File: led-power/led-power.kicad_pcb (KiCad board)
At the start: 2 copper layers, 86.4 x 86.4 mm, 88 parts, among them J1 String1, J10 PowerInput, J11 Qwiic, J12 Qwiic, J2 String2, J3 String3, J4 String4, J5 String5, J6 String6, J7 String7, J8 String8, J9 PowerInput, Q1 Q_NMOS_GDS, Q2 Q_NMOS_GDS, Q3 Q_NMOS_GDS, Q4 Q_NMOS_GDS, Q5 Q_NMOS_GDS, Q6 Q_NMOS_GDS, Q7 Q_NMOS_GDS, Q8 Q_NMOS_GDS, U1 MCP6V51, U10 L78L05ACZ-AP, U11 MCP1501, U2 MCP6V51, U3 MCP6V51, U4 MCP6V51, U5 MCP6V51, U6 MCP6V51, U7 MCP6V51, U8 MCP6V51, U9 MCP23017_SO

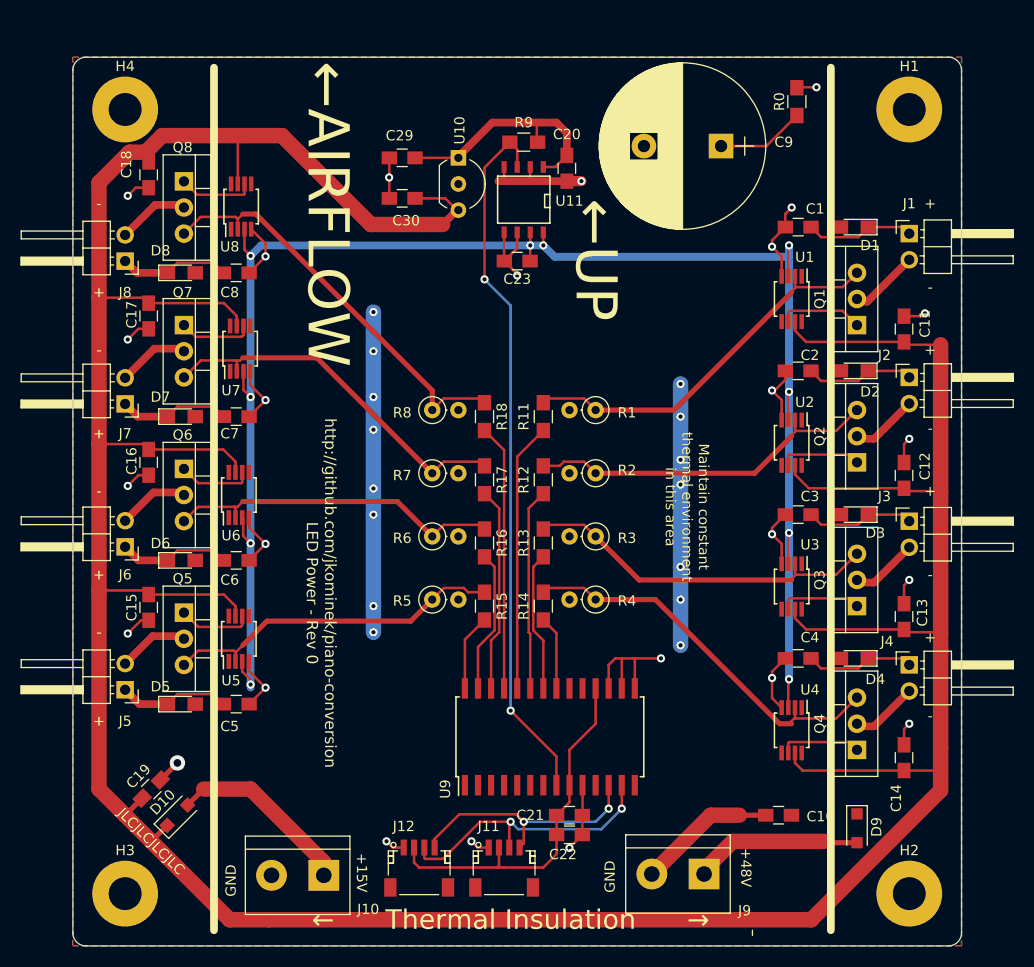
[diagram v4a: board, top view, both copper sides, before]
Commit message: Made I2C address configurable to match other boards, tweaked silkscreen
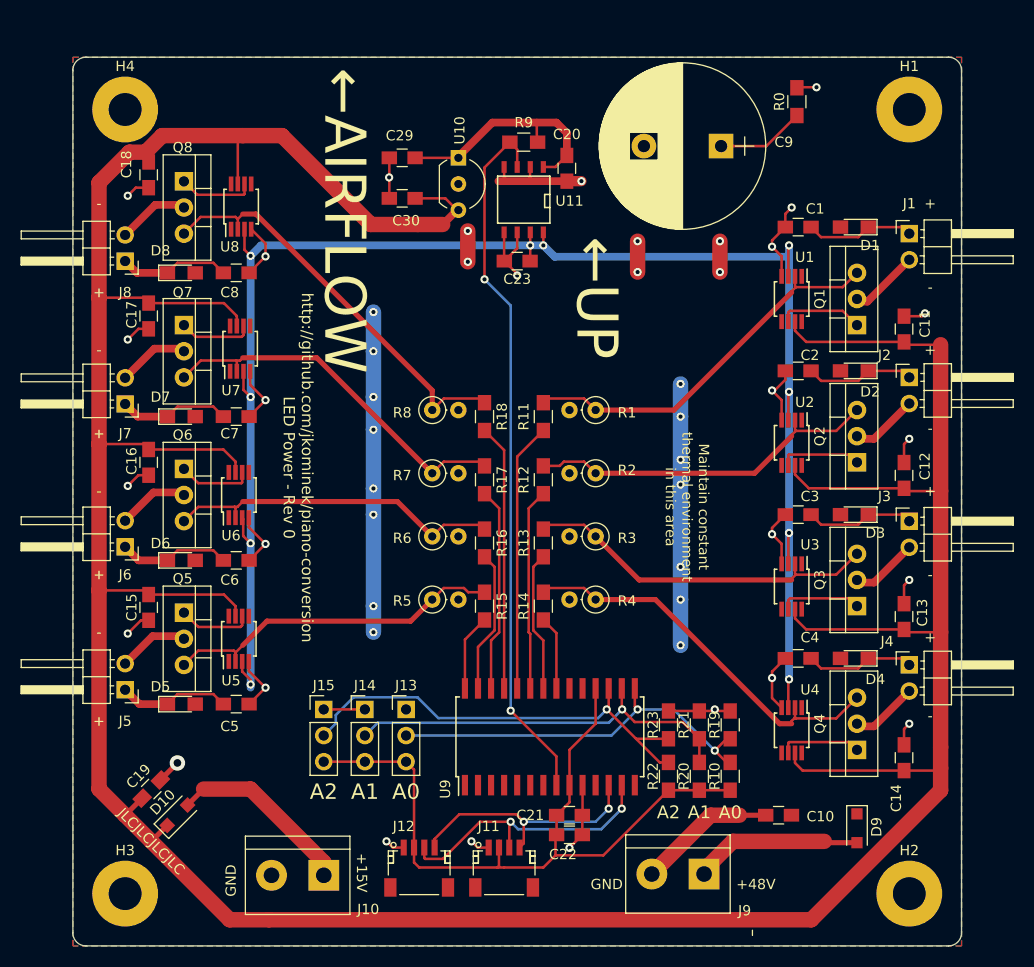
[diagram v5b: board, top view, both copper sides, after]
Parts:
- added J13: A0, Pin_Headers:Pin_Header_Straight_1x03_Pitch2.54mm, F.Cu at (103.5, 134.5)
- added J14: A1, Pin_Headers:Pin_Header_Straight_1x03_Pitch2.54mm, F.Cu at (99.5, 134.5)
- added J15: A2, Pin_Headers:Pin_Header_Straight_1x03_Pitch2.54mm, F.Cu at (95.5, 134.5)
- added R10: DNP, Resistors_SMD:R_0805_HandSoldering, F.Cu at (135.0, 141.0)
- added R19: DNP, Resistors_SMD:R_0805_HandSoldering, F.Cu at (135.0, 136.0)
- added R20: DNP, Resistors_SMD:R_0805_HandSoldering, F.Cu at (132.0, 141.0)
- added R21: DNP, Resistors_SMD:R_0805_HandSoldering, F.Cu at (132.0, 136.0)
- added R22: DNP, Resistors_SMD:R_0805_HandSoldering, F.Cu at (129.0, 141.0)
- added R23: DNP, Resistors_SMD:R_0805_HandSoldering, F.Cu at (129.0, 136.0)
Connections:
- U9 pad 15: GND -> /A0
- U9 pad 16: GND -> /A1
- U9 pad 17: GND -> /A2
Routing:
- net /A2: track 0.00 -> 44.1 mm, vias 0 -> 1
- net /A1: track 0.00 -> 39.1 mm, vias 0 -> 1
- net /A0: track 0.00 -> 38.8 mm, vias 0 -> 2
- net +3V3: track 36.4 -> 72.6 mm
- net GND: track 131.0 -> 136.7 mm, vias 26 -> 32
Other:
- board text added: "A0"
- board text added: "A1"
- board text added: "A2"
- board text removed: "← Thermal Insulation →"

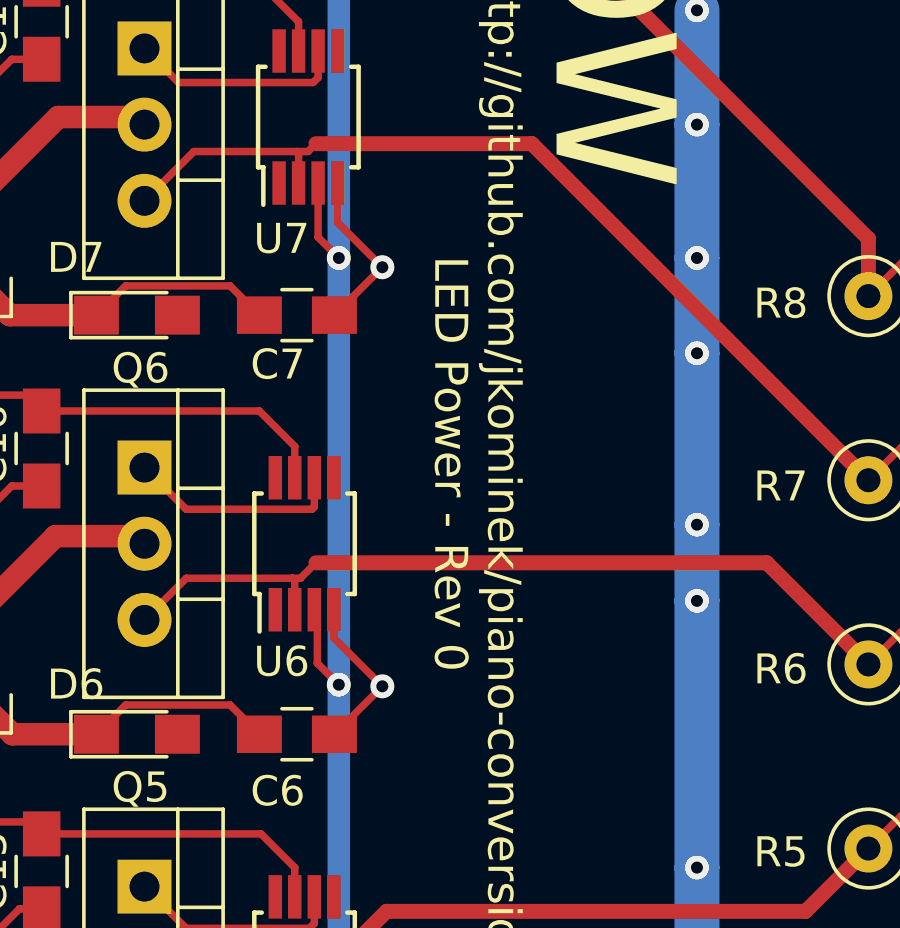
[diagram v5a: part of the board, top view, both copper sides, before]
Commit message: Add/update board rev silkscreen, nothing else
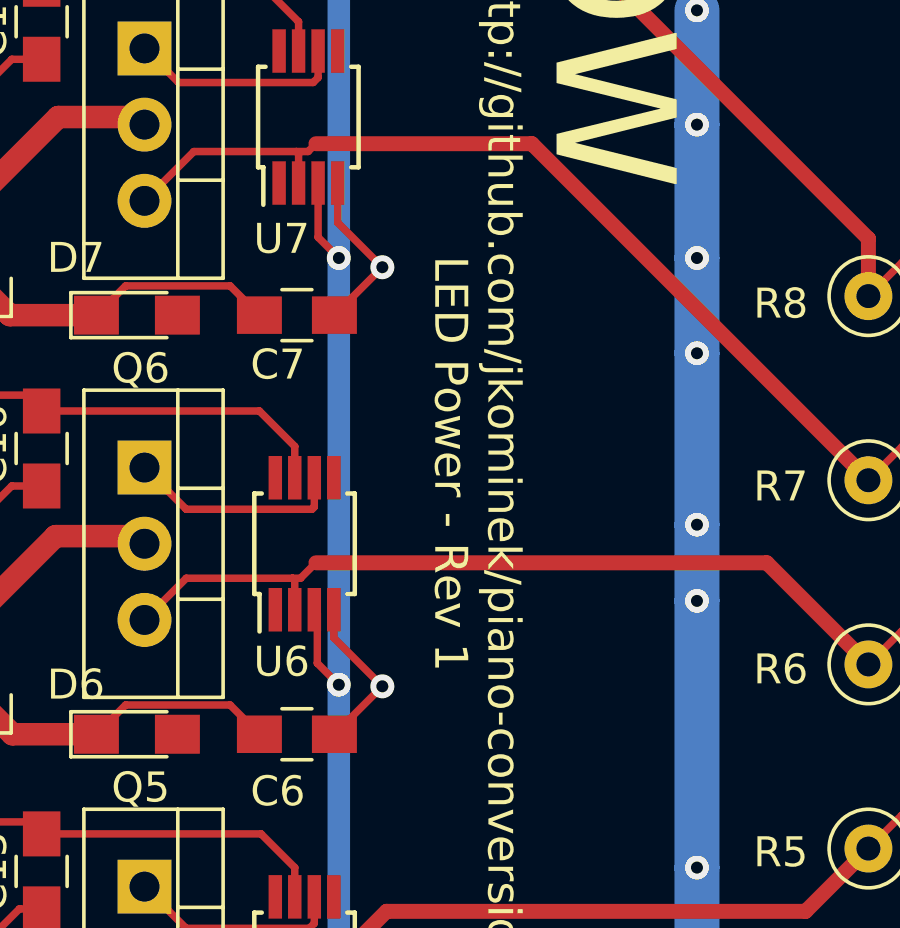
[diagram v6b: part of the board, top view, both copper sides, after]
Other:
- board text added: "http://github.com/jkominek/piano-conversion LED Power - Rev 1"
- board text removed: "http://github.com/jkominek/piano-conversion LED Power - Rev 0"

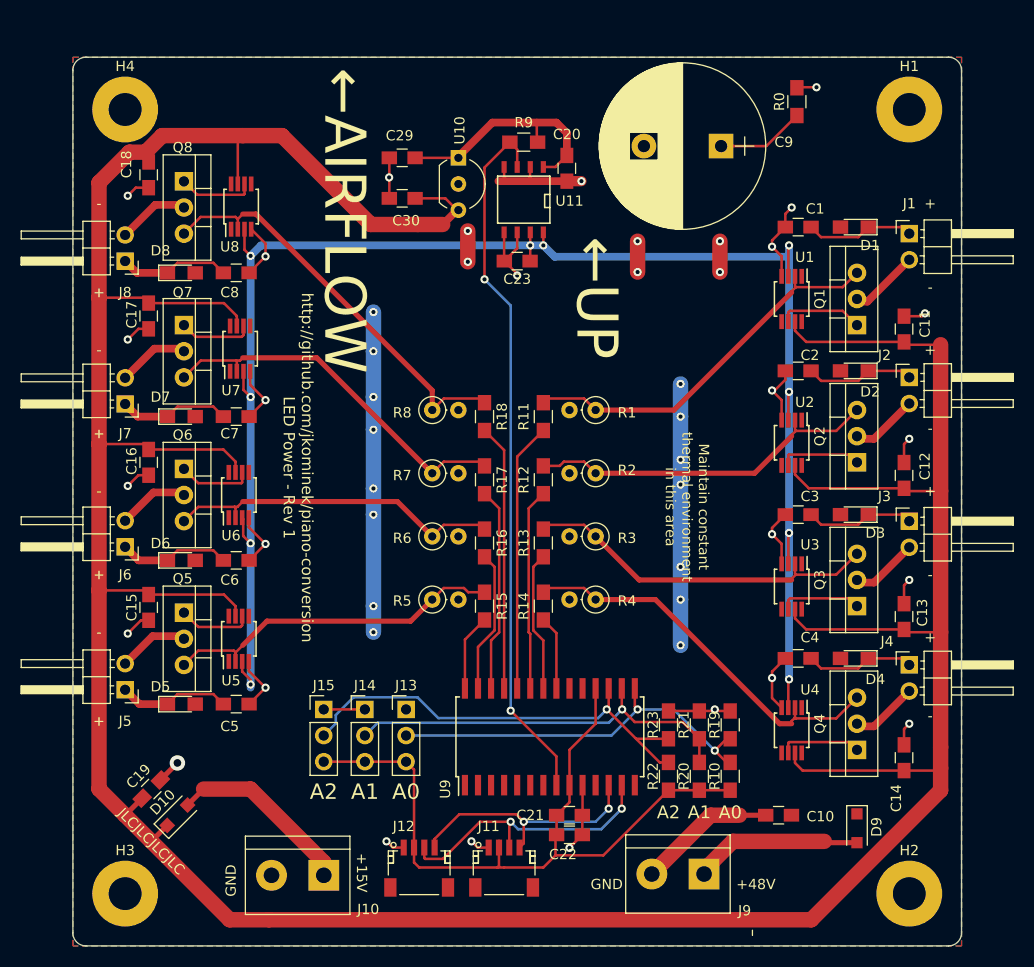
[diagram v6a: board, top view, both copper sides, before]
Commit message: Rev 2 changes
* Pulldown on VREF so that ~SHDN can work
* Voltage dividers on the rails, fed to the MCP23017 so it can detect faults
* Increased space between Qwiic headers
* Bring I2C bus out on 0.100" header
* Tweaked LED positions on the left side; right seemed to be fine.
* Converted it to a four layer board. +15V/GND/GND/+48V
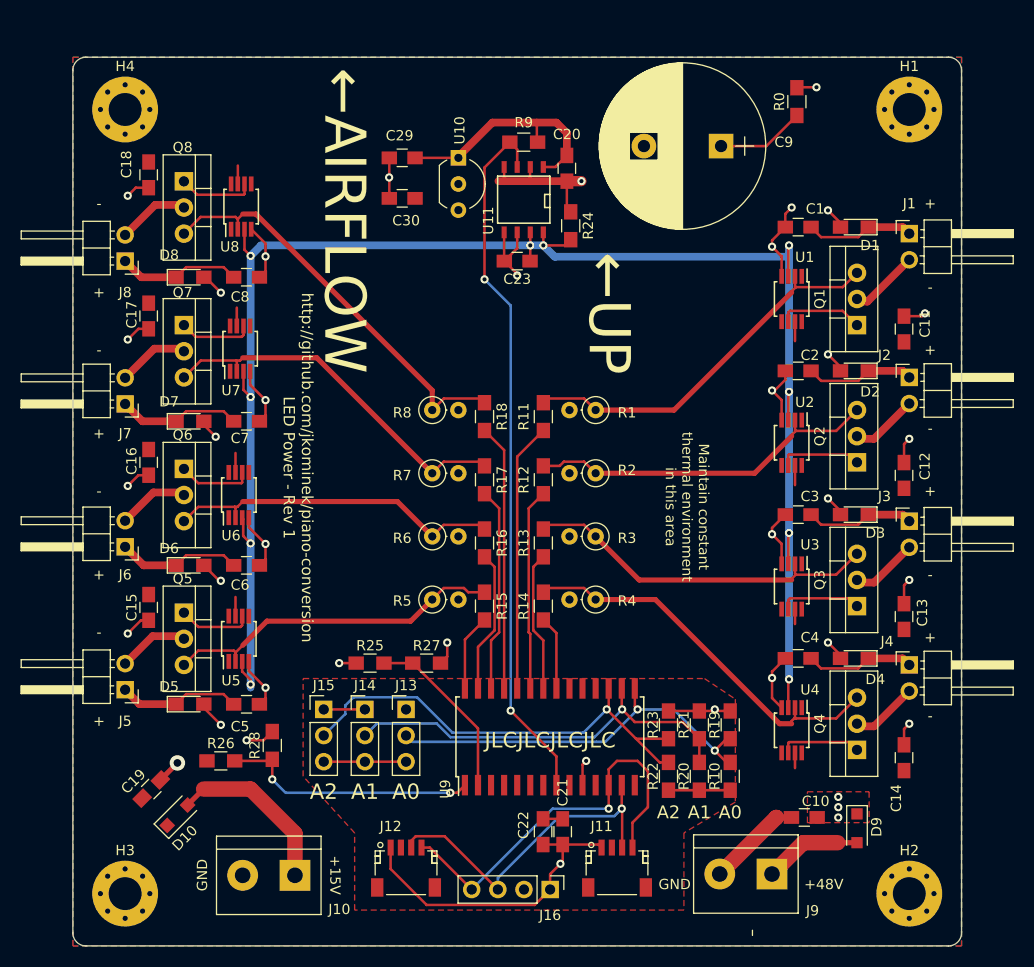
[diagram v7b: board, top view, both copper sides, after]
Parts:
- added J16: I2C Header, Pin_Headers:Pin_Header_Straight_1x04_Pitch2.54mm, F.Cu at (117.5, 152.0)
- added R24: 2400, Resistors_SMD:R_0805_HandSoldering, F.Cu at (119.5, 87.5)
- added R25: 4700, Resistors_SMD:R_0805_HandSoldering, F.Cu at (100.0, 130.0)
- added R26: 1300, Resistors_SMD:R_0805_HandSoldering, F.Cu at (85.5, 139.5)
- added R27: 330, Resistors_SMD:R_0805_HandSoldering, F.Cu at (105.5, 130.0)
- added R28: 330, Resistors_SMD:R_0805_HandSoldering, F.Cu at (90.5, 138.0)
- H1, H2, H3, H4: footprint Mounting_Holes:MountingHole_3.2mm_M3_Pad -> Mounting_Holes:MountingHole_3.2mm_M3_Pad_Via
- moved J11 11.0 mm to (124.0, 149.9)
- moved J9 6.60 mm to (139.1, 150.5)
- moved J10 2.80 mm to (92.7, 150.6)
- moved C22 2.58 mm to (116.8, 146.4), turned to 270 degrees
- moved C10 2.51 mm to (142.2, 145.0)
- moved C21 1.73 mm to (118.7, 146.4), turned to 270 degrees
- moved J12 1.28 mm to (103.5, 149.9)
- moved C6 1.12 mm to (88.0, 120.5)
- moved C7 1.10 mm to (88.0, 106.5)
- moved C8 1.09 mm to (88.0, 92.5)
- moved C5 1.01 mm to (88.0, 134.0)
- moved D6 0.97 mm to (82.5, 120.5)
- moved D7 0.95 mm to (82.5, 106.5)
- moved D8 0.94 mm to (82.5, 92.5)
- moved D5 0.84 mm to (82.5, 134.0)
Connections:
- U9 pad 1: (no net) -> /15V_SENSE
- U9 pad 2: (no net) -> /48V_SENSE
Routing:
- net +15V: track 358.4 -> 14.3 mm
- net +3V3: track 72.6 -> 15.9 mm
- net +48V: track 65.1 -> 27.8 mm, vias 15 -> 12
- net /15V_SENSE: track 0.00 -> 25.2 mm, vias 0 -> 2
- net /48V_SENSE: track 0.00 -> 17.3 mm
- net GND: track 136.7 -> 153.8 mm, vias 32 -> 27
- net /SCL: track 24.5 -> 39.6 mm, vias 2 -> 1
- net Net-(D9-Pad2): track 16.5 -> 9.52 mm
- net /SDA: track 27.7 -> 33.4 mm, vias 2 -> 1
- net /VREF: track 164.1 -> 167.0 mm
- net Net-(C6-Pad1): track 10.9 -> 12.1 mm
- net Net-(C7-Pad1): track 10.9 -> 12.1 mm
- net Net-(C8-Pad1): track 10.8 -> 12.0 mm
- net /A2: track 44.1 -> 45.3 mm
- net Net-(D10-Pad2): track 18.1 -> 16.9 mm
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- added copper zone on In2.Cu, net (none)
- added copper zone on F.Cu, net +15V
- added copper zone on F.Cu, net +3V3
- added copper zone on B.Cu, net +48V
- added copper zone on In1.Cu, net GND
- removed copper zone on B.Cu, net GND
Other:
- copper layers 2 -> 4

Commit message: Add ~IRQ header, lots of trace cleanup. Bump the board rev
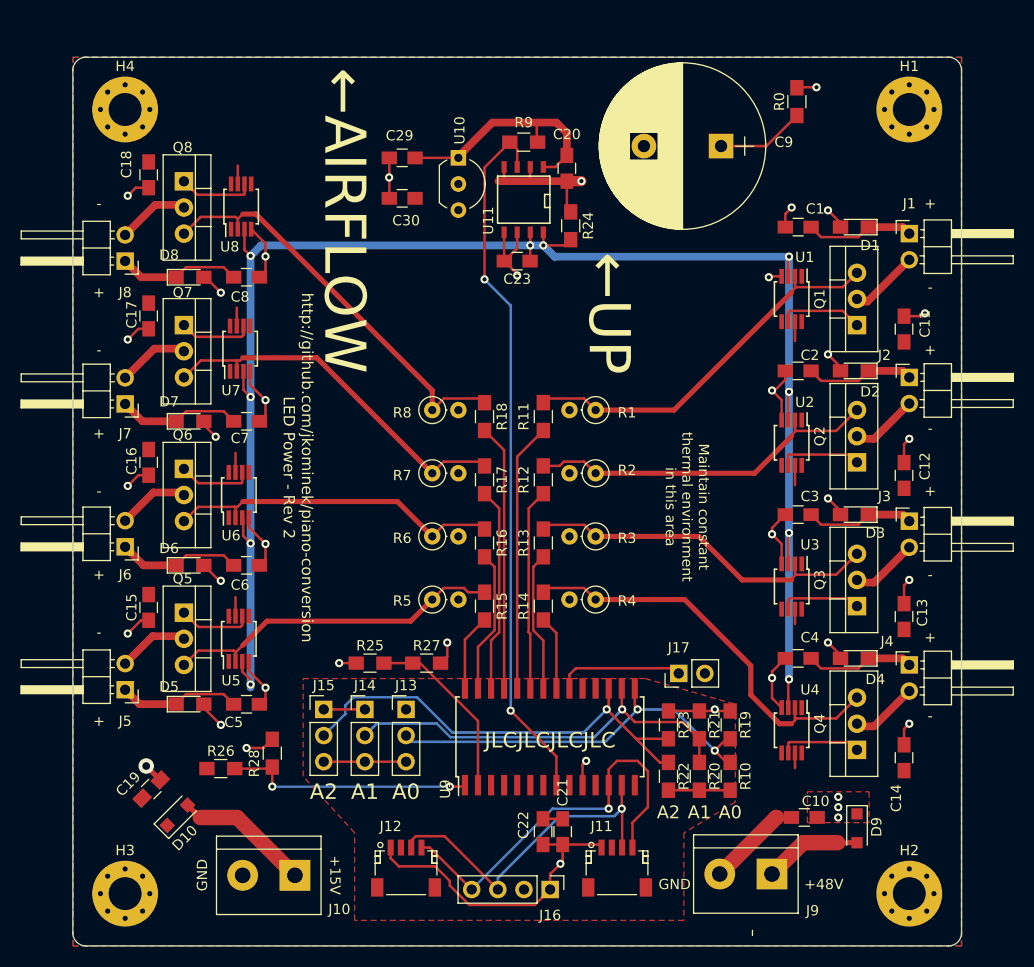
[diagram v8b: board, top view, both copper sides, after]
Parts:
- added J17: IRQ, Pin_Headers:Pin_Header_Straight_1x02_Pitch2.54mm, F.Cu at (130.0, 131.0)
- moved R26 0.75 mm to (85.5, 140.2)
- moved R28 0.75 mm to (90.5, 138.8)
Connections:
- U9 pad 20: (no net) -> /~IRQ
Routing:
- net /~IRQ: track 0.00 -> 12.4 mm
- net GND: track 153.8 -> 148.6 mm
- net Net-(D10-Pad2): track 16.9 -> 13.3 mm
- net /VREF: track 167.0 -> 164.8 mm
- net /Feedback4: track 38.6 -> 40.3 mm
- net /15V_SENSE: track 25.2 -> 24.4 mm
- added copper zone on In2.Cu, net GND
- removed copper zone on In2.Cu, net (none)
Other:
- board text added: "http://github.com/jkominek/piano-conversion LED Power - Rev 2"
- board text removed: "http://github.com/jkominek/piano-conversion LED Power - Rev 1"
